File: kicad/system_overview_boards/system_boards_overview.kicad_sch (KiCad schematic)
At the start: 0 parts

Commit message: up
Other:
- sheet Main PSU PCB ports: added GND/HEATER-; removed HEATER-
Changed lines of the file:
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@@
 	)
 	(junction
+		(at 88.9 78.74)
+		(diameter 0)
+		(color 0 0 0 0)
+	)
+	(junction
 		(at 140.97 127)
 		(diameter 0)
@@
 	)
 	(junction
-		(at 85.09 63.5)
-		(diameter 0)
-		(color 0 0 0 0)
-	)
-	(junction
 		(at 184.15 59.69)
 		(diameter 0)
@@
 	)
 	(junction
-		(at 101.6 109.22)
-		(diameter 0)
-		(color 0 0 0 0)
-	)
-	(junction
-		(at 101.6 83.82)
-		(diameter 0)
-		(color 0 0 0 0)
-	)
-	(junction
 		(at 186.69 54.61)
 		(diameter 0)
@@
 	(wire
 		(pts
+			(xy 101.6 83.82) (xy 119.38 83.82)
+		)
+		(stroke
+			(width 0)
+			(type default)
+		)
+	)
+	(wire
+		(pts
 			(xy 242.57 104.14) (xy 229.87 104.14)
 		)
@@
 	(wire
 		(pts
+			(xy 101.6 109.22) (xy 128.27 109.22)
+		)
+		(stroke
+			(width 0)
+			(type default)
+		)
+	)
+	(wire
+		(pts
 			(xy 187.96 67.31) (xy 199.39 67.31)
 		)
@@
 	(wire
 		(pts
-			(xy 100.33 109.22) (xy 100.33 107.95)
-		)
-		(stroke
-			(width 0)
-			(type default)
-		)
-	)
-	(wire
-		(pts
 			(xy 199.39 127) (xy 186.69 127)
 		)
@@
 	(wire
 		(pts
-			(xy 101.6 63.5) (xy 85.09 63.5)
-		)
-		(stroke
-			(width 0)
-			(type default)
-		)
-	)
-	(wire
-		(pts
 			(xy 233.68 124.46) (xy 236.22 124.46)
 		)
@@
 	(wire
 		(pts
-			(xy 101.6 109.22) (xy 100.33 109.22)
-		)
-		(stroke
-			(width 0)
-			(type default)
-		)
-	)
-	(wire
-		(pts
 			(xy 139.7 124.46) (xy 139.7 133.35)
 		)
@@
 	(wire
 		(pts
-			(xy 101.6 109.22) (xy 128.27 109.22)
-		)
-		(stroke
-			(width 0)
-			(type default)
-		)
-	)
-	(wire
-		(pts
 			(xy 38.1 113.03) (xy 35.56 113.03)
 		)
@@
 	(wire
 		(pts
-			(xy 101.6 78.74) (xy 101.6 63.5)
+			(xy 88.9 78.74) (xy 88.9 63.5)
 		)
 		(stroke
@@
 	(wire
 		(pts
-			(xy 50.8 63.5) (xy 85.09 63.5)
+			(xy 50.8 63.5) (xy 88.9 63.5)
 		)
 		(stroke
@@
 	(wire
 		(pts
-			(xy 100.33 107.95) (xy 90.17 107.95)
-		)
-		(stroke
-			(width 0)
-			(type default)
-		)
-	)
-	(wire
-		(pts
 			(xy 64.77 127) (xy 69.85 127)
 		)
@@
 	(wire
 		(pts
-			(xy 85.09 82.55) (xy 85.09 63.5)
+			(xy 88.9 82.55) (xy 88.9 78.74)
 		)
 		(stroke
@@
 	(wire
 		(pts
-			(xy 90.17 81.28) (xy 118.11 81.28)
+			(xy 92.71 81.28) (xy 118.11 81.28)
 		)
 		(stroke
@@
 	(wire
 		(pts
-			(xy 93.98 91.44) (xy 93.98 85.09)
-		)
-		(stroke
-			(width 0)
-			(type default)
-		)
-	)
-	(wire
-		(pts
 			(xy 265.43 104.14) (xy 265.43 119.38)
 		)
@@
 	(wire
 		(pts
-			(xy 93.98 85.09) (xy 101.6 85.09)
-		)
-		(stroke
-			(width 0)
-			(type default)
-		)
-	)
-	(wire
-		(pts
 			(xy 241.3 60.96) (xy 241.3 62.23)
 		)
@@
 	(wire
 		(pts
-			(xy 90.17 82.55) (xy 90.17 81.28)
+			(xy 92.71 82.55) (xy 92.71 81.28)
 		)
 		(stroke
@@
 	(wire
 		(pts
-			(xy 90.17 107.95) (xy 90.17 91.44)
-		)
-		(stroke
-			(width 0)
-			(type default)
-		)
-	)
-	(wire
-		(pts
 			(xy 140.97 80.01) (xy 140.97 86.36)
 		)
@@
 	(wire
 		(pts
-			(xy 134.62 78.74) (xy 101.6 78.74)
+			(xy 134.62 78.74) (xy 88.9 78.74)
 		)
 		(stroke
@@
 	(wire
 		(pts
-			(xy 90.17 91.44) (xy 93.98 91.44)
-		)
-		(stroke
-			(width 0)
-			(type default)
-		)
-	)
-	(wire
-		(pts
 			(xy 139.7 124.46) (xy 146.05 124.46)
 		)
@@
 	(wire
 		(pts
-			(xy 101.6 83.82) (xy 119.38 83.82)
-		)
-		(stroke
-			(width 0)
-			(type default)
-		)
-	)
-	(wire
-		(pts
 			(xy 62.23 118.11) (xy 69.85 118.11)
 		)
@@
 		)
 	)
-	(wire
-		(pts
-			(xy 101.6 85.09) (xy 101.6 83.82)
-		)
-		(stroke
-			(width 0)
-			(type default)
-		)
-	)
 	(arc
 		(start 109.22 78.74)
@@
 		)
 		(pin "BIAS" passive
-			(at 90.17 82.55 90)
+			(at 92.71 82.55 90)
 			(effects
 				(font
@@
 		)
 		(pin "CHASSIS{slash}PE" passive
-			(at 85.09 82.55 90)
+			(at 88.9 82.55 90)
 			(effects
 				(font
@@
 			)
 		)
-		(pin "HEATER-" passive
-			(at 101.6 109.22 0)
+		(pin "B-" passive
+			(at 101.6 88.9 0)
 			(effects
 				(font
@@
 			)
 		)
-		(pin "B-" passive
-			(at 101.6 88.9 0)
+		(pin "B2-" passive
+			(at 101.6 91.44 0)
 			(effects
 				(font
@@
 			)
 		)
-		(pin "B2-" passive
-			(at 101.6 91.44 0)
+		(pin "GND{slash}HEATER-" passive
+			(at 101.6 109.22 0)
 			(effects
 				(font

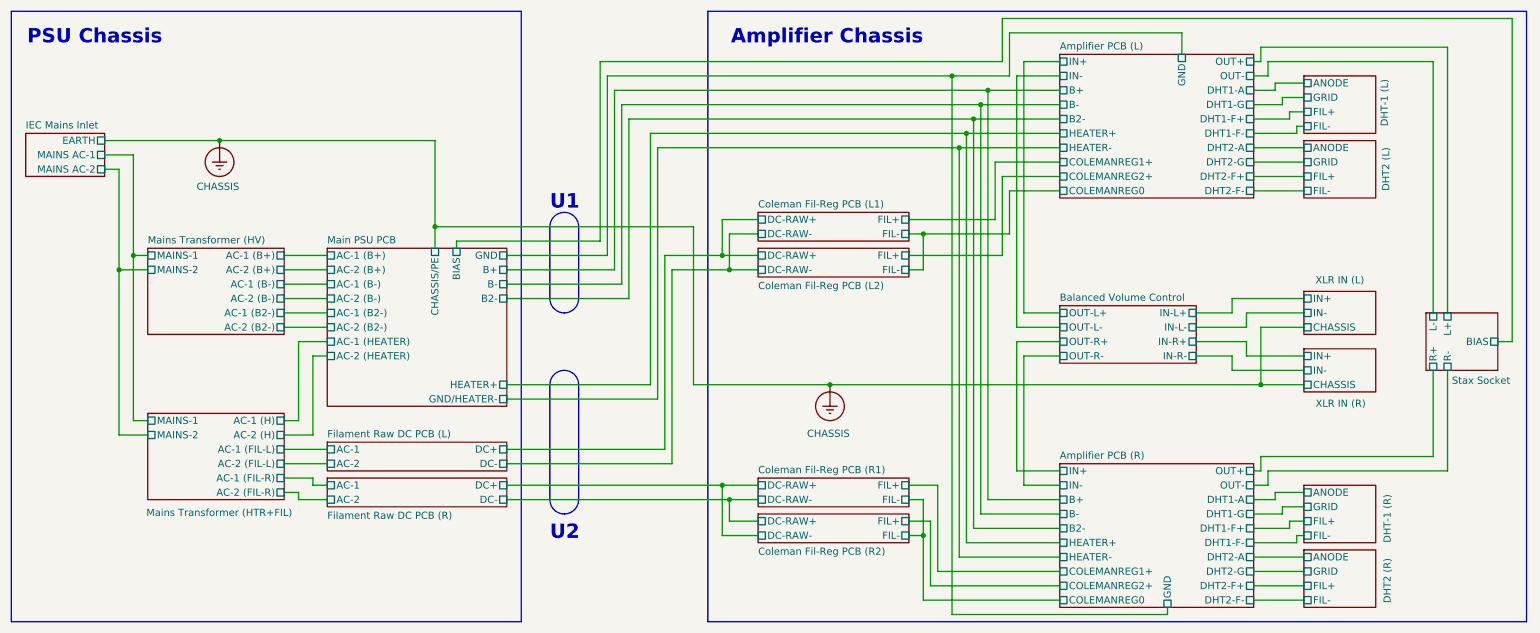
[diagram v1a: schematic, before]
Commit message: Power indicator LEDs in system overview diagram
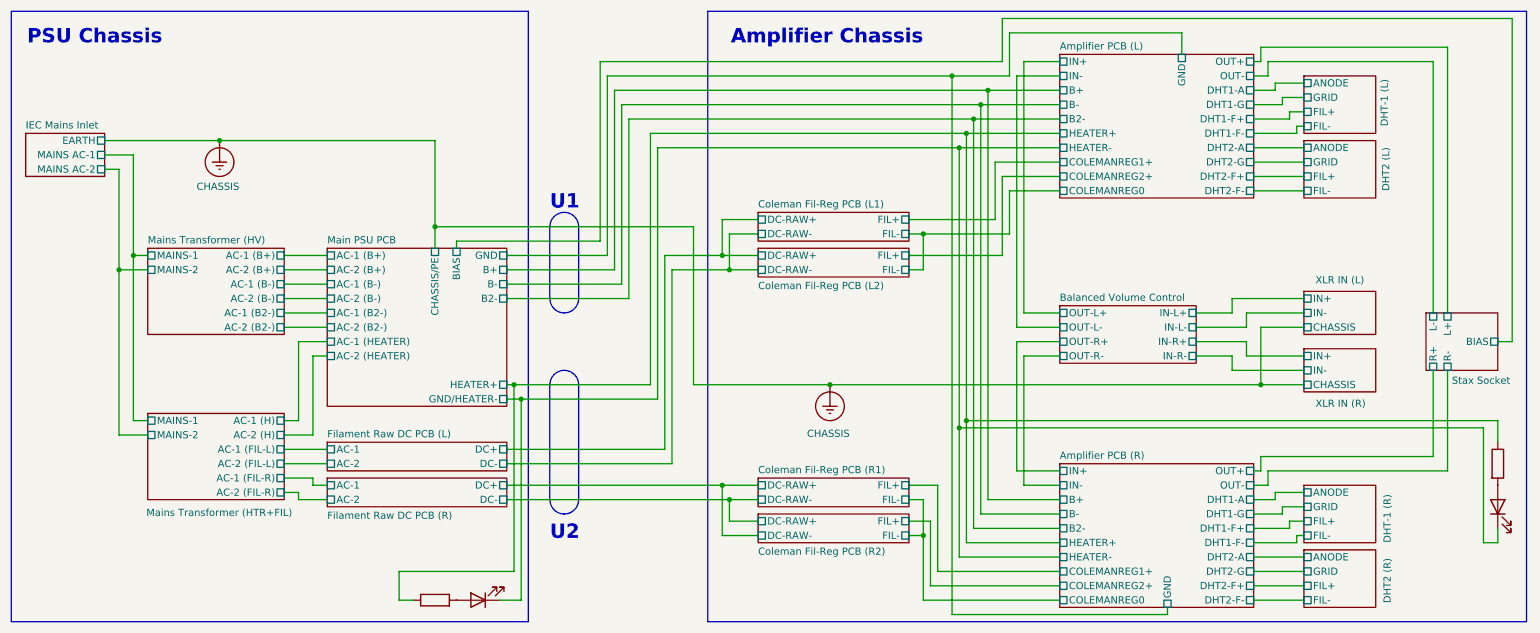
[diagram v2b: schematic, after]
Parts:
- added D1, D2: LED, symbol Device:LED
- added R1, R2: ~, symbol Device:R
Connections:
- net Amplifier PCB (L)/HEATER+: now also R1.1, R2.1
- net Amplifier PCB (L)/HEATER-: now also D1.1 (K), D2.1 (K)
- new net: D1.2 (A), R1.2
- new net: D2.2 (A), R2.2

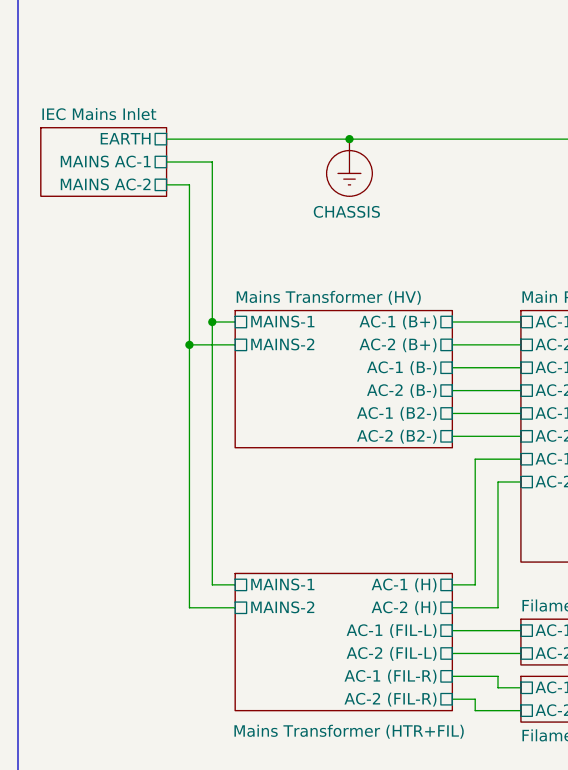
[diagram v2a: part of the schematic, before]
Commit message: mains inlet details, #24, #25
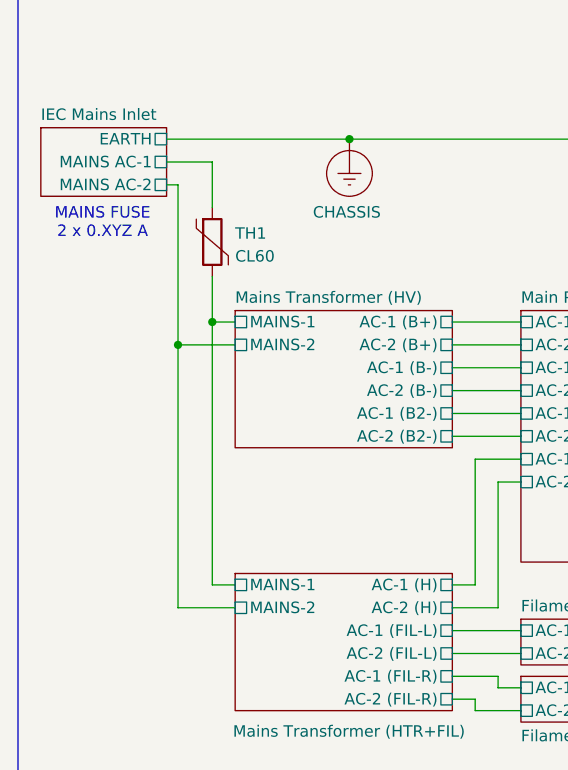
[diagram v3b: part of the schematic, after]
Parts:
- added TH1: CL60, symbol Device:Thermistor_NTC
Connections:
- net IEC Mains Inlet/MAINS AC-1: now also TH1.1
- new net Mains Transformer (HTR+FIL)/MAINS-1: TH1.2
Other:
- note added: "MAINS FUSE 2 x 0.XYZ A"

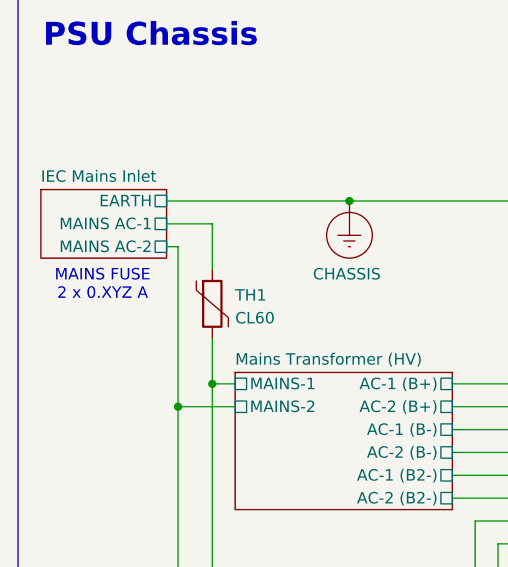
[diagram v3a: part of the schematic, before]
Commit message: fuse rating in overview schemtaic #24 #25
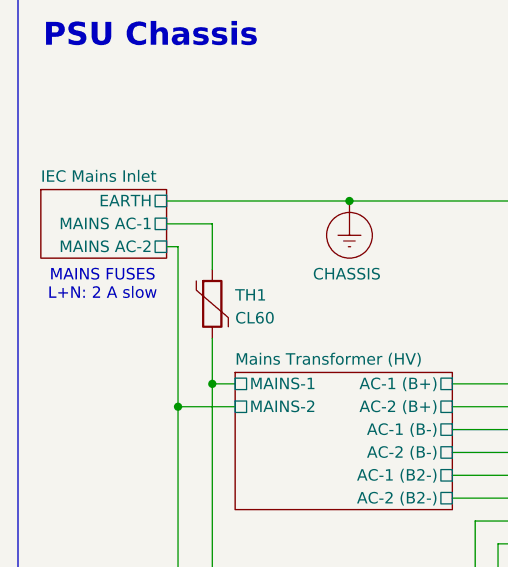
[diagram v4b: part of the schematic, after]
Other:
- note added: "MAINS FUSES L+N: 2 A slow"
- note removed: "MAINS FUSE 2 x 0.XYZ A"
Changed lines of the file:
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@@
 		)
 	)
-	(text "MAINS FUSE\n2 x 0.XYZ A"
+	(text "MAINS FUSES\nL+N: 2 A slow"
 		(exclude_from_sim no)
 		(at 23.368 72.898 0)
